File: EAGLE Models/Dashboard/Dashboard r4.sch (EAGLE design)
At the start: 125 parts, among them IC1 AT90CAN128, IC2 MCP2551SO8, IC3 NUP2105L, IC5 FT232RL, Q1 56P2859, U1 74LCX125M

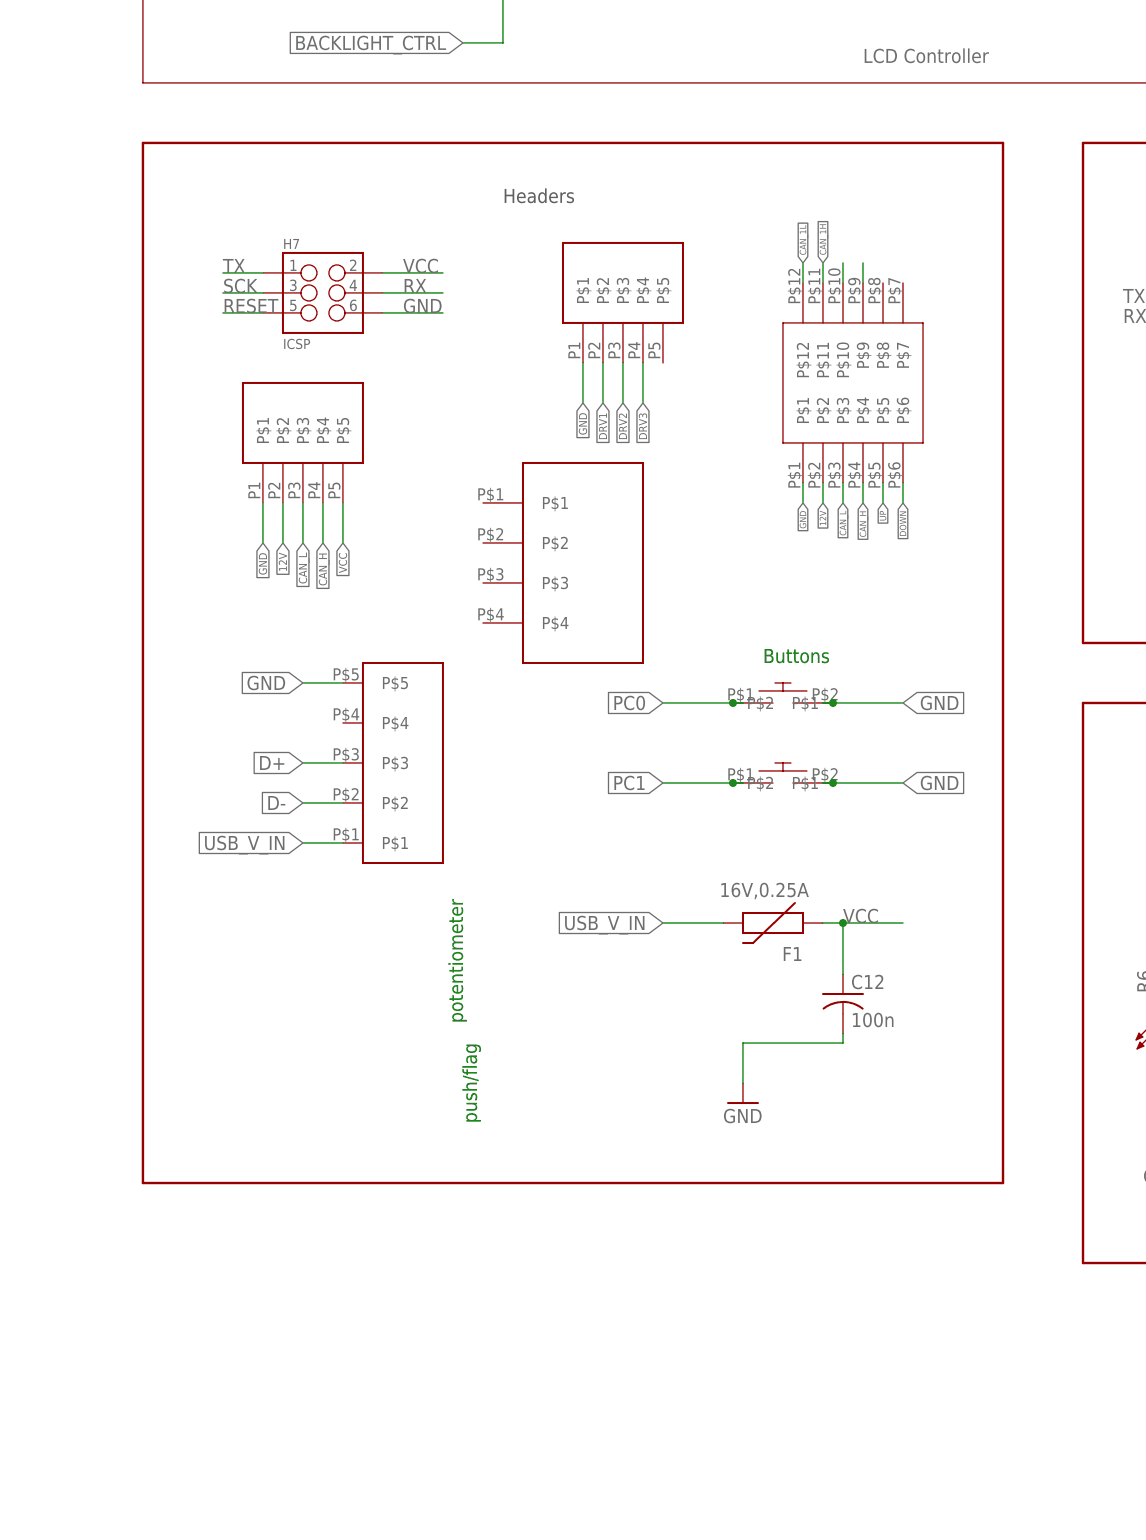
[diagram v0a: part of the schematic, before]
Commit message: Continued work on dashboard connector
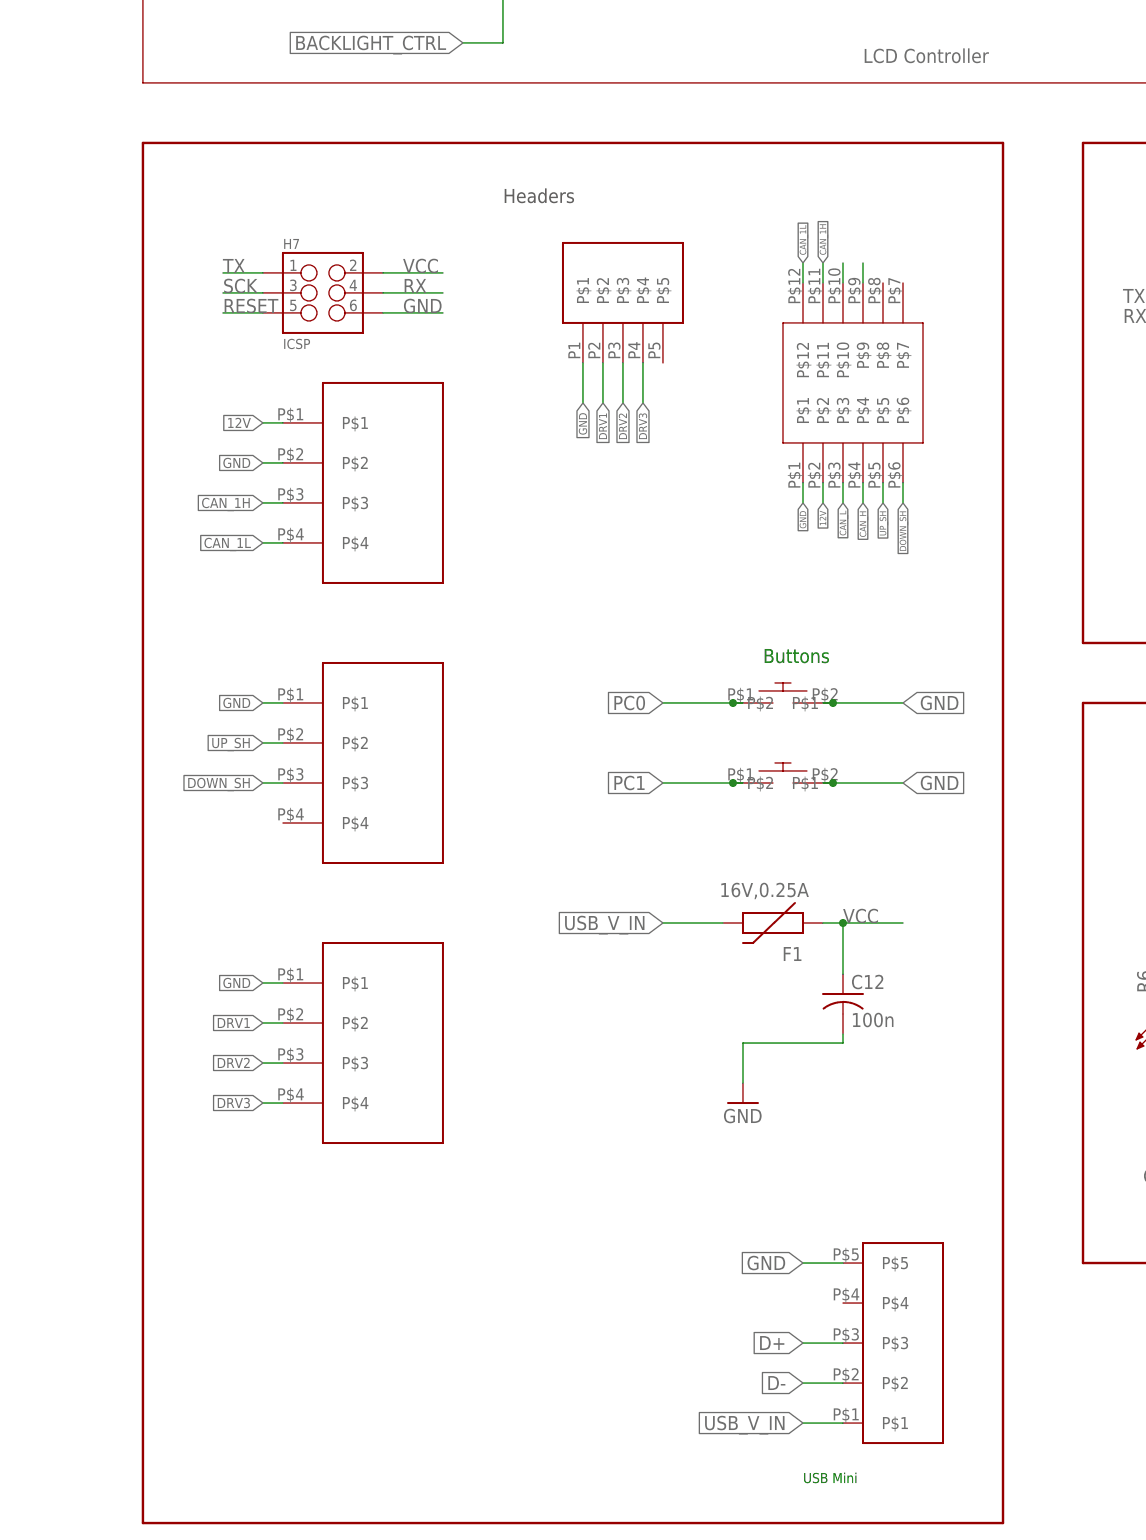
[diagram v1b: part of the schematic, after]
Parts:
- removed CANPWR: MICRO5LOCK, DashAndCAN library:MICRO5LOCK
- added U$23, U$24: 043650-0409, molex:043650-0409
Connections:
- removed net DOWN: U$21.P$6
- removed net UP: U$21.P$5
- new net DOWN_SH: U$21.P$6, U$23.P$3
- new net UP_SH: U$21.P$5, U$23.P$2
- net 12V: now also U$22.P$1; no longer CANPWR.P$2
- net CAN_1H: now also U$22.P$3
- net CAN_1L: now also U$22.P$4
- net CAN_H: no longer CANPWR.P$4
- net CAN_L: no longer CANPWR.P$3
- net DRV1: now also U$24.P$2
- net DRV2: now also U$24.P$3
- net DRV3: now also U$24.P$4
- net GND: now also U$22.P$2, U$23.P$1, U$24.P$1; no longer CANPWR.P$1
- net VCC: no longer CANPWR.P$5
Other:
- note added: "USB Mini"
- note removed: "potentiometer"
- note removed: "push/flag"

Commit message: Continuing board layout
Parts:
- removed C15: 10uF, resistor:C-US025-024X044
- removed C3, C4: 22uF, resistor:C-US025-024X044
- removed D2: 1N5819, diode:1N5819-B
- removed L2: 22uH, inductors:DR73
- removed LEDOUT: MICRO5LOCK, DashAndCAN library:MICRO5LOCK
- removed U$1: V7805-1000, formula electric:V78XX-1000
- added C23, C24: 10uF, rcl:C-USC0603
- added D3: 1N5819, diode:1N5819-BSOD123
- added U$26: NCP1117, on-semiconductor:NCP1117
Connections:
- net CAN_H renamed CAN_0H
- net CAN_L renamed CAN_0L
- removed net N$13: C3.1, L2.1, U$1.OUT
- new net 5V_REG_IN: C23.1, D3.C, U$26.INPUT
- net 12V: now also D3.A; no longer D2.A
- net 12V_PROTECTED: no longer C15.1, D2.C, U$1.IN
- net CAN_1H: now also U$21.P$7; no longer U$21.P$11
- net CAN_1L: now also U$21.P$8; no longer U$21.P$12
- net DRV1: no longer LEDOUT.P$2
- net DRV2: no longer LEDOUT.P$3
- net DRV3: no longer LEDOUT.P$4
- net GND: now also C23.2, C24.2, U$26.ADJUST; no longer C15.2, C3.2, C4.2, LEDOUT.P$1, U$1.GND
- net VCC: now also C24.1, U$26.OUTPUT; no longer C4.1, L2.2

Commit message: Everything organized, placed on the board ready for traces
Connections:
- net BACKLIGHT_CTRL: no longer U$18.SHDN
- net CAN_0H: now also U$21.P$3; no longer U$21.P$4
- net CAN_0L: now also U$21.P$4; no longer U$21.P$3
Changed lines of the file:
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@@
 <net name="BACKLIGHT_CTRL" class="0">
-<segment>
-<wire x1="137.16" y1="99.06" x2="129.54" y2="99.06" width="0.1524" layer="91"/>
-<label x="129.54" y="99.06" size="1.778" layer="95" rot="R180" xref="yes"/>
-<pinref part="U$18" gate="G$1" pin="SHDN"/>
-</segment>
 <segment>
 <pinref part="U$2" gate="A" pin="BACKLIGHT"/>
@@
 <net name="CAN_0L" class="1">
 <segment>
-<pinref part="U$21" gate="G$1" pin="P$3"/>
-<wire x1="-307.34" y1="111.76" x2="-307.34" y2="109.22" width="0.1524" layer="91"/>
-<label x="-307.34" y="109.22" size="0.8128" layer="95" rot="R270" xref="yes"/>
-</segment>
-<segment>
 <wire x1="-236.22" y1="132.08" x2="-226.06" y2="132.08" width="0.1524" layer="91"/>
 <wire x1="-226.06" y1="124.46" x2="-226.06" y2="132.08" width="0.1524" layer="91"/>
@@
 <label x="-207.01" y="132.08" size="1.778" layer="95" xref="yes"/>
 </segment>
-</net>
-<net name="CAN_0H" class="1">
 <segment>
 <pinref part="U$21" gate="G$1" pin="P$4"/>
@@
 <label x="-304.8" y="109.22" size="0.8128" layer="95" rot="R270" xref="yes"/>
 </segment>
+</net>
+<net name="CAN_0H" class="1">
 <segment>
 <wire x1="-220.98" y1="127" x2="-236.22" y2="127" width="0.1524" layer="91"/>
@@
 <junction x="-220.98" y="127"/>
 </segment>
-</net>
+<segment>
+<pinref part="U$21" gate="G$1" pin="P$3"/>
+<wire x1="-307.34" y1="111.76" x2="-307.34" y2="109.22" width="0.1524" layer="91"/>
+<label x="-307.34" y="109.22" size="0.8128" layer="95" rot="R270" xref="yes"/>
+</segment>
+</net>

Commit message: 1st Revision of board layout done!!
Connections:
- net 12V: now also U$21.P$4; no longer U$21.P$2
- net CAN_0H: now also U$21.P$2; no longer U$21.P$3
- net CAN_0L: now also U$21.P$3; no longer U$21.P$4
- net PB6(PWM): now also R16.1; no longer R14.1
- net PB7(PWM): now also R14.1; no longer R16.1
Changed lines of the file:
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@@
 </segment>
 <segment>
-<pinref part="R16" gate="G$1" pin="1"/>
-<wire x1="-468.63" y1="41.91" x2="-472.44" y2="41.91" width="0.1524" layer="91"/>
-<label x="-472.44" y="41.91" size="1.778" layer="95" rot="R180" xref="yes"/>
+<pinref part="R14" gate="G$1" pin="1"/>
+<wire x1="-468.63" y1="115.57" x2="-472.44" y2="115.57" width="0.1524" layer="91"/>
+<label x="-472.44" y="115.57" size="1.778" layer="95" rot="R180" xref="yes"/>
 </segment>
 </net>
@@
 </segment>
 <segment>
-<pinref part="R14" gate="G$1" pin="1"/>
-<wire x1="-468.63" y1="115.57" x2="-472.44" y2="115.57" width="0.1524" layer="91"/>
-<label x="-472.44" y="115.57" size="1.778" layer="95" rot="R180" xref="yes"/>
+<pinref part="R16" gate="G$1" pin="1"/>
+<wire x1="-468.63" y1="41.91" x2="-472.44" y2="41.91" width="0.1524" layer="91"/>
+<label x="-472.44" y="41.91" size="1.778" layer="95" rot="R180" xref="yes"/>
 </segment>
 </net>
@@
 <net name="12V" class="2">
 <segment>
-<pinref part="U$21" gate="G$1" pin="P$2"/>
-<wire x1="-309.88" y1="111.76" x2="-309.88" y2="109.22" width="0.1524" layer="91"/>
-<label x="-309.88" y="109.22" size="0.8128" layer="95" rot="R270" xref="yes"/>
-</segment>
-<segment>
 <pinref part="U$22" gate="G$1" pin="P$1"/>
 <wire x1="-378.46" y1="119.38" x2="-381" y2="119.38" width="0.1524" layer="91"/>
@@
 <wire x1="-241.3" y1="68.58" x2="-248.92" y2="68.58" width="0.1524" layer="91"/>
 <label x="-248.92" y="68.58" size="1.778" layer="95" rot="R180" xref="yes"/>
+</segment>
+<segment>
+<pinref part="U$21" gate="G$1" pin="P$4"/>
+<wire x1="-304.8" y1="111.76" x2="-304.8" y2="109.22" width="0.1524" layer="91"/>
+<label x="-304.8" y="109.22" size="0.8128" layer="95" rot="R270" xref="yes"/>
 </segment>
 </net>
@@
 </segment>
 <segment>
-<pinref part="U$21" gate="G$1" pin="P$4"/>
-<wire x1="-304.8" y1="111.76" x2="-304.8" y2="109.22" width="0.1524" layer="91"/>
-<label x="-304.8" y="109.22" size="0.8128" layer="95" rot="R270" xref="yes"/>
+<pinref part="U$21" gate="G$1" pin="P$3"/>
+<wire x1="-307.34" y1="111.76" x2="-307.34" y2="109.22" width="0.1524" layer="91"/>
+<label x="-307.34" y="109.22" size="0.8128" layer="95" rot="R270" xref="yes"/>
 </segment>
 </net>
@@
 </segment>
 <segment>
-<pinref part="U$21" gate="G$1" pin="P$3"/>
-<wire x1="-307.34" y1="111.76" x2="-307.34" y2="109.22" width="0.1524" layer="91"/>
-<label x="-307.34" y="109.22" size="0.8128" layer="95" rot="R270" xref="yes"/>
-</segment>
-</net>
+<pinref part="U$21" gate="G$1" pin="P$2"/>
+<wire x1="-309.88" y1="111.76" x2="-309.88" y2="109.22" width="0.1524" layer="91"/>
+<label x="-309.88" y="109.22" size="0.8128" layer="95" rot="R270" xref="yes"/>
+</segment>
+</net>

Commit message: Revision 2. Organization overhaul. Added ground plane, vias
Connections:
- removed net N$76: BL_L2.1, CIN10.1, CIN12.1, CIN5.1, CIN9.1, RCOMM2.2
- removed net SCK: H7.3
- net 12V: now also BL_L2.1, CIN10.1, CIN12.1, CIN5.1, CIN9.1, RCOMM2.2
- net AVR_SCLK: now also H7.3
- net PF1: now also U$17.P$13; no longer U$16.P$13
- net PF2: now also U$16.P$13; no longer U$17.P$13

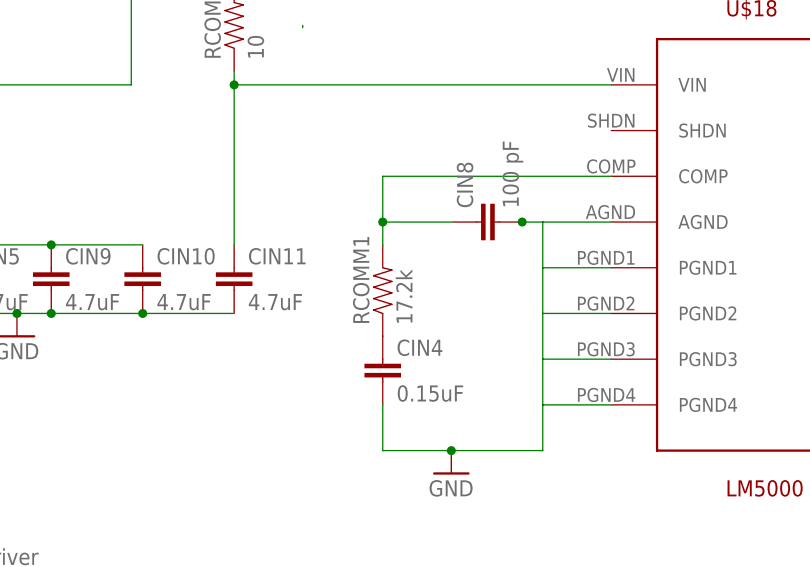
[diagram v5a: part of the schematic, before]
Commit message: Added correct cut-tape resistors
Updated Tape and Reel resistors to Cut Tape
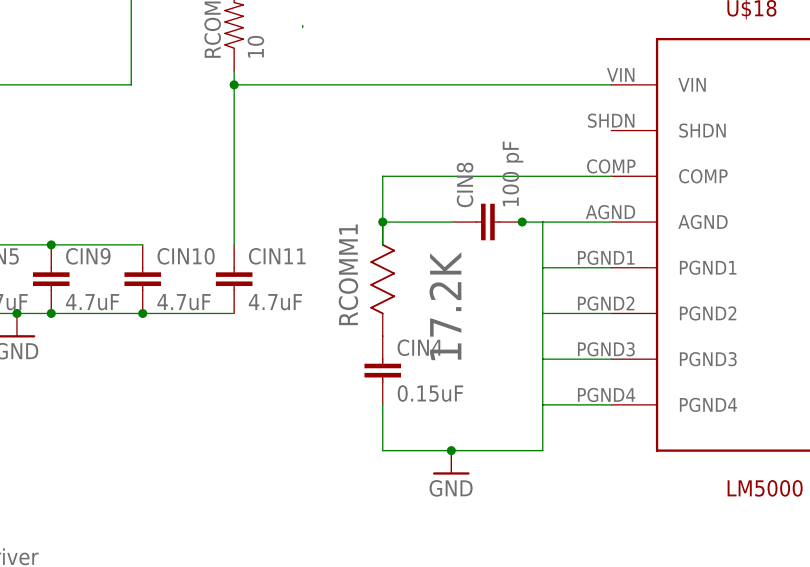
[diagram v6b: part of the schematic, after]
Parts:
- RCOMM1: value 17.2k -> 17.2K; device SparkFun-Resistors:RESISTOR0603 -> Vishay_By_element14_Batch_1:TNPW12062K00BEEN
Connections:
- removed net N$74: CIN4.1, RCOMM1.1
- new net N$4: CIN4.1, RCOMM1.2
- net N$75: now also RCOMM1.1; no longer RCOMM1.2
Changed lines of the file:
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@@
 <?xml version="1.0" encoding="utf-8"?>
 <!DOCTYPE eagle SYSTEM "eagle.dtd">
-<eagle version="8.3.2">
+<eagle version="8.4.0">
 <drawing>
 <settings>
@@
 <layer number="56" name="wert" color="7" fill="1" visible="no" active="no"/>
 <layer number="57" name="tCAD" color="7" fill="1" visible="no" active="no"/>
+<layer number="88" name="SimResults" color="9" fill="1" visible="yes" active="yes"/>
+<layer number="89" name="SimProbes" color="9" fill="1" visible="yes" active="yes"/>
 <layer number="90" name="Modules" color="5" fill="1" visible="yes" active="yes"/>
 <layer number="91" name="Nets" color="2" fill="1" visible="yes" active="yes"/>
@@
 <part name="CIN6" library="SparkFun-Capacitors" deviceset="CAP" device="0805" value="10uF"/>
 <part name="CIN7" library="SparkFun-Capacitors" deviceset="CAP" device="0805" value="0.1uF"/>
-<part name="RCOMM1" library="SparkFun-Resistors" deviceset="RESISTOR" device="0603" value="17.2k"/>
 <part name="BL_L2" library="tdk" deviceset="LTF4022-D" device="" value="15uH"/>
 <part name="GND21" library="SparkFun-Aesthetics" deviceset="GND" device=""/>
@@
 <part name="C23" library="rcl" deviceset="C-US" device="C0603" value="10uF"/>
 <part name="C24" library="rcl" deviceset="C-US" device="C0603" value="10uF"/>
+<part name="RCOMM1" library="Vishay_By_element14_Batch_1" deviceset="TNPW12062K00BEEN" device="" value="17.2K"/>
 </parts>
 <sheets>
@@
 <instance part="CIN6" gate="G$1" x="184.15" y="73.914" rot="R90"/>
 <instance part="CIN7" gate="G$1" x="183.896" y="68.58" rot="R90"/>
-<instance part="RCOMM1" gate="G$1" x="111.76" y="81.28" rot="R90"/>
 <instance part="BL_L2" gate="A" x="146.05" y="118.11" rot="R90"/>
 <instance part="GND21" gate="1" x="119.38" y="60.96"/>
@@
 <instance part="C23" gate="G$1" x="-233.68" y="60.96"/>
 <instance part="C24" gate="G$1" x="-182.88" y="60.96"/>
+<instance part="RCOMM1" gate="A" x="111.76" y="76.2" rot="R90"/>
 </instances>
 <busses>
@@
 </segment>
 </net>
-<net name="N$74" class="0">
-<segment>
-<pinref part="CIN4" gate="G$1" pin="1"/>
-<pinref part="RCOMM1" gate="G$1" pin="1"/>
-</segment>
-</net>
 <net name="N$75" class="0">
 <segment>
 <pinref part="CIN8" gate="G$1" pin="1"/>
 <wire x1="119.634" y1="88.9" x2="111.76" y2="88.9" width="0.1524" layer="91"/>
-<pinref part="RCOMM1" gate="G$1" pin="2"/>
 <wire x1="111.76" y1="88.9" x2="111.76" y2="86.36" width="0.1524" layer="91"/>
 <pinref part="U$18" gate="G$1" pin="COMP"/>
@@
 <wire x1="111.76" y1="93.98" x2="111.76" y2="88.9" width="0.1524" layer="91"/>
 <junction x="111.76" y="88.9"/>
+<pinref part="RCOMM1" gate="A" pin="1"/>
 </segment>
 </net>
@@
 </segment>
 </net>
+<net name="N$4" class="0">
+<segment>
+<pinref part="CIN4" gate="G$1" pin="1"/>
+<pinref part="RCOMM1" gate="A" pin="2"/>
+</segment>
+</net>
